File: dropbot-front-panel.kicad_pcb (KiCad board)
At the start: 4 copper layers, 108 x 68.8 mm, 22 parts, among them P1 SFM-105-02-L-D-A, P10 CONN_01X02, P13 CONN_01X01, P14 CONN_01X01, P15 CONN_01X01, P2 SFM-125-02-L-D-A, P3 TFM-125-02-L-DH, P4 SFM-125-02-L-D-A, P5 TFM-125-02-L-DH, P6 SFM-125-02-L-D-A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

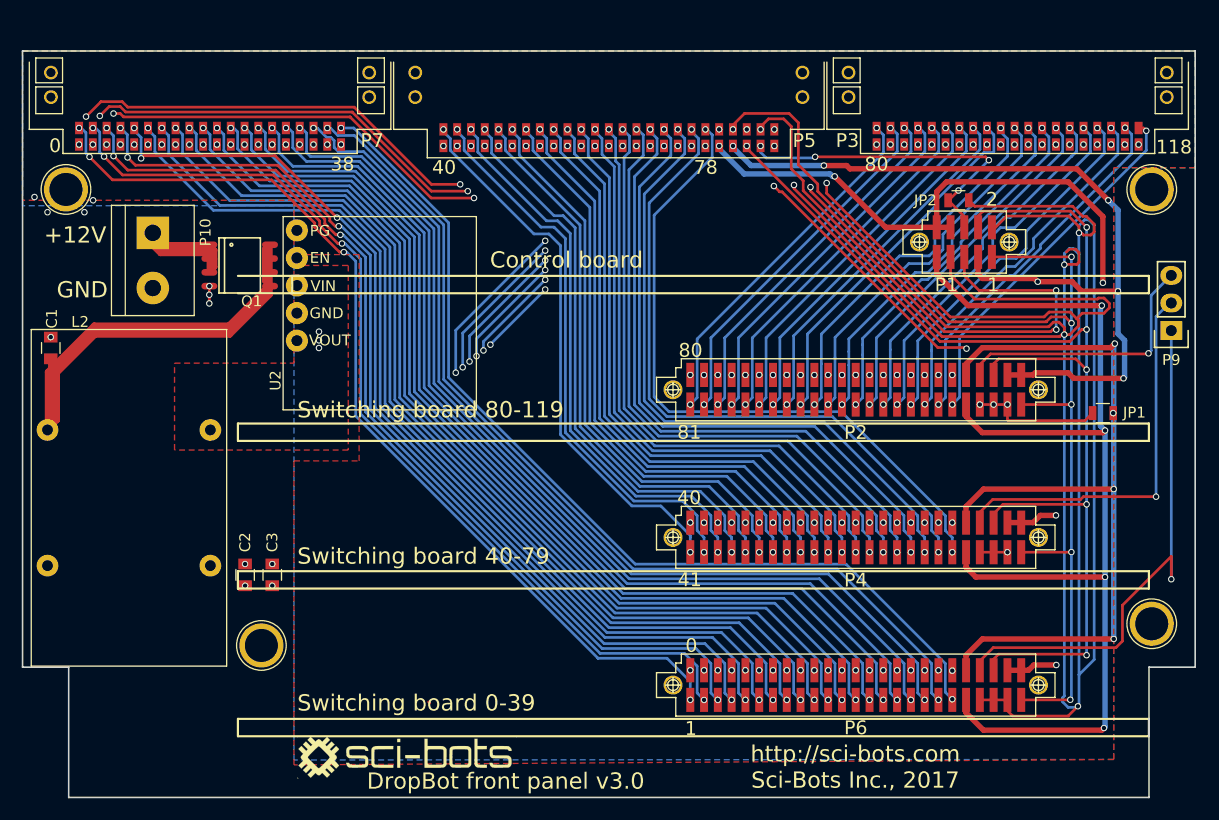
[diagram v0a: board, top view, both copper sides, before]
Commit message: Fix #1, #2 and #3
1. Add i2c EEPROM chip to store serial number, hardware version, etc.
2. Move C2 and C3 (they currently collide with the 2nd switching board)
3. Fix reverse polarity protection
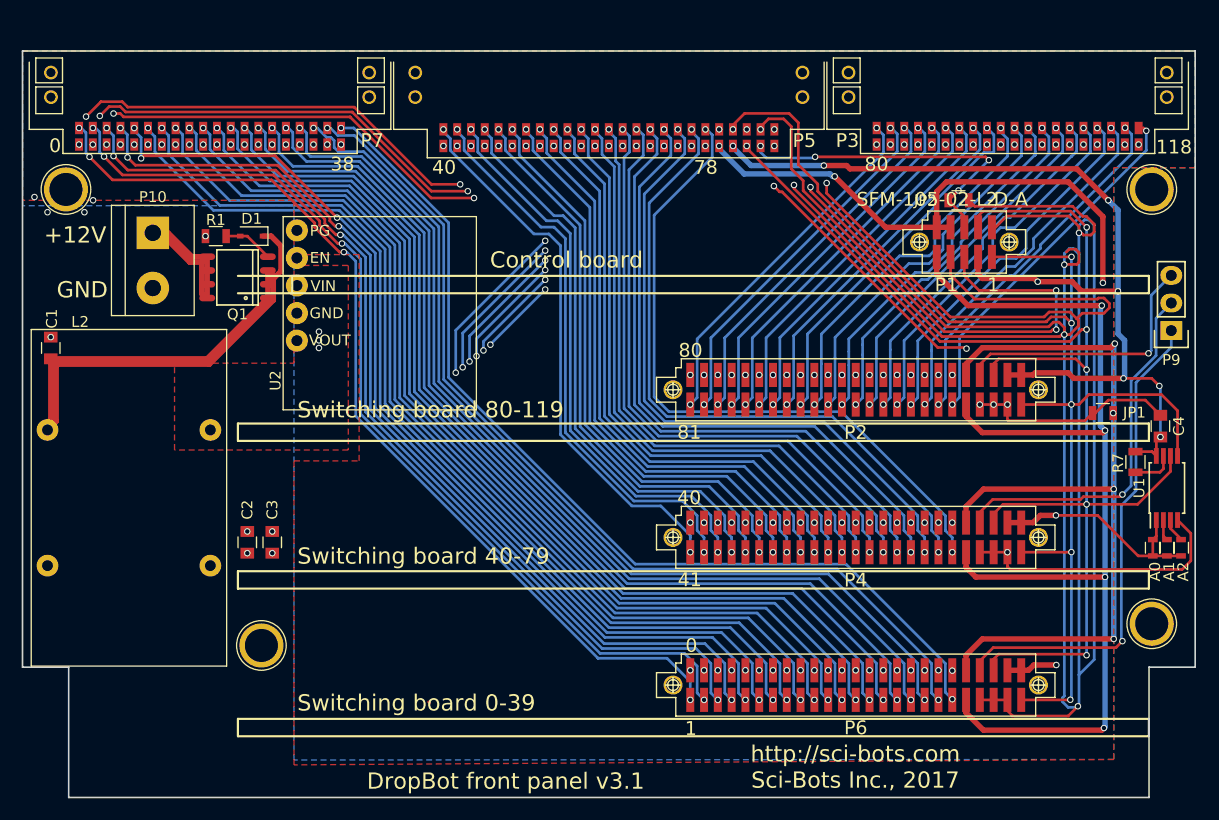
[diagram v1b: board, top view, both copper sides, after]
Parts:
- removed G***: LOGO, WheelerLab:SCI-BOTS-LOGO
- added C4: 0.1uF, Capacitors_SMD:C_0805, F.Cu at (150.8, 65.8)
- added D1: 10V, Diodes_SMD:D_SOD-323, F.Cu at (67.1, 48.3)
- added JP3: A0, Resistors_SMD:R_0603, F.Cu at (150.1, 77.0)
- added JP4: A1, Resistors_SMD:R_0603, F.Cu at (151.4, 77.0)
- added JP5: A2, Resistors_SMD:R_0603, F.Cu at (152.7, 77.0)
- added R1: 10k, Resistors_SMD:R_0805, F.Cu at (63.8, 48.3)
- added R7: 10k, Resistors_SMD:R_0805, F.Cu at (148.5, 69.1)
- added U1: CAT24C__, Housings_SSOP:TSSOP-8_4.4x3mm_Pitch0.65mm, F.Cu at (151.4, 71.5)
- P1: footprint SFM-105-02-XXX-D-A -> WheelerLab:SFM-105-02-XXX-D-A
- P3, P7: value TFM-125-02-L-DH -> TFM-120-02-L-DH
- moved C2 3.01 mm to (66.7, 76.5)
- moved C3 3.00 mm to (69.0, 76.5)
- moved Q1 1.12 mm to (65.8, 52.1), turned to 90 degrees
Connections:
- Q1 pad 1: +12V_SUPPLY -> Net-(C1-Pad1)
- Q1 pad 2: +12V_SUPPLY -> Net-(C1-Pad1)
- Q1 pad 3: +12V_SUPPLY -> Net-(C1-Pad1)
- Q1 pad 4: CHASIS_GND -> Net-(D1-Pad2)
- Q1 pad 5: Net-(C1-Pad1) -> +12V_SUPPLY
- Q1 pad 6: Net-(C1-Pad1) -> +12V_SUPPLY
- Q1 pad 7: Net-(C1-Pad1) -> +12V_SUPPLY
- Q1 pad 8: Net-(C1-Pad1) -> +12V_SUPPLY
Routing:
- net GND: track 300.1 -> 330.3 mm
- net +3.3V: track 94.6 -> 123.4 mm, vias 11 -> 13
- net Net-(C1-Pad1): track 96.7 -> 71.8 mm
- net SDA: track 105.1 -> 120.1 mm
- net SCL: track 123.1 -> 133.5 mm
- net Net-(D1-Pad2): track 0.00 -> 4.63 mm
- net RST1: track 50.4 -> 46.2 mm
- net Net-(R7-Pad2): track 0.00 -> 3.88 mm
- net +12V_SUPPLY: track 24.1 -> 20.3 mm
- net Net-(JP5-Pad2): track 0.00 -> 2.20 mm
- net RST2: track 36.3 -> 34.3 mm
- net Net-(JP4-Pad2): track 0.00 -> 1.93 mm
- net CHASIS_GND: track 13.2 -> 11.4 mm, vias 10 -> 8
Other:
- net class Default: clearance 0.2 -> 0.16
- rule trace_clearance: 0.2 -> 0.16
- board text added: "DropBot front panel v3.1"
- board text removed: "DropBot front panel v3.0"

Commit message: Update to use Sci-Bots library
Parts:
- L2: footprint WheelerLab:RN242-X-02-XXX -> Sci-Bots:RN242-X-02-XXX
- P1: footprint WheelerLab:SFM-105-02-XXX-D-A -> Sci-Bots:SFM-105-02-XXX-D-A
- P10: value CONN_01X02 -> Conn_01x02
- P13, P14, P15, P8: value CONN_01X01 -> Conn_01x01
- P2, P4, P6: footprint WheelerLab:SFM-125-02-XXX-D-A -> Sci-Bots:SFM-125-02-XXX-D-A
- P3, P7: footprint WheelerLab:TFM-120-02-X-DH -> Sci-Bots:TFM-120-02-X-DH
- P5: footprint WheelerLab:TFM-125-02-X-DH -> Sci-Bots:TFM-125-02-X-DH
- P9: value CONN_01X03 -> Conn_01x03
- U2: footprint WheelerLab:D24V22F -> Sci-Bots:D24V22F
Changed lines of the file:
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@@
-(kicad_pcb (version 4) (host pcbnew 4.0.6)
+(kicad_pcb (version 4) (host pcbnew 4.0.7)
   (general
     (links 217)
@@
   (layers
     (0 F.Cu signal)
-    (1 PWR power)
-    (2 GND power)
+    (1 PWR power hide)
+    (2 GND power hide)
     (31 B.Cu signal)
     (32 B.Adhes user)
@@
     (add_net "Net-(C1-Pad1)")
   )
-  (module WheelerLab:RN242-X-02-XXX (layer F.Cu)
+  (module Sci-Bots:RN242-X-02-XXX (layer F.Cu)
     (at 55.8 72.4)
     (fp_text reference L2 (at -4.5 -16.2) (layer F.SilkS)
@@
       (effects (font (size 1 1) (thickness 0.15)))
     )
-    (fp_text value CONN_01X03 (at 2.2 2.7 270) (layer F.Fab) hide
+    (fp_text value Conn_01x03 (at 2.2 2.7 270) (layer F.Fab) hide
       (effects (font (size 1 1) (thickness 0.15)))
     )
@@
     )
   )
-  (module WheelerLab:TFM-120-02-X-DH (layer F.Cu)
+  (module Sci-Bots:TFM-120-02-X-DH (layer F.Cu)
     (at 63.2716 31.7638)
     (descr "0.050\" DOUBLE HORIZONTAL TERMINAL STRIP.")
@@
       (net 2 GND))
   )
-  (module WheelerLab:TFM-120-02-X-DH (layer F.Cu)
+  (module Sci-Bots:TFM-120-02-X-DH (layer F.Cu)
     (at 136.7284 31.7638)
     (descr "0.050\" DOUBLE HORIZONTAL TERMINAL STRIP.")
@@
       (effects (font (size 1 1) (thickness 0.15)))
     )
-    (fp_text value CONN_01X02 (at 2.2 6.4 270) (layer F.Fab) hide
+    (fp_text value Conn_01x02 (at 2.2 6.4 270) (layer F.Fab) hide
       (effects (font (size 1 1) (thickness 0.15)))
     )
@@
     )
   )
-  (module WheelerLab:TFM-125-02-X-DH (layer F.Cu)
+  (module Sci-Bots:TFM-125-02-X-DH (layer F.Cu)
     (at 100 31.7638)
     (descr "0.050\" DOUBLE HORIZONTAL TERMINAL STRIP.")
@@
     )
   )
-  (module WheelerLab:D24V22F (layer F.Cu)
+  (module Sci-Bots:D24V22F (layer F.Cu)
     (at 70 46.5 270)
     (fp_text reference U2 (at 15.1 0.7 450) (layer F.SilkS)
@@
       (effects (font (size 1 1) (thickness 0.15)))
     )
-    (fp_text value CONN_01X01 (at 1.1 3.3) (layer F.Fab) hide
+    (fp_text value Conn_01x01 (at 1.1 3.3) (layer F.Fab) hide
       (effects (font (size 1 1) (thickness 0.15)))
     )
@@
       (effects (font (size 1 1) (thickness 0.15)))
     )
-    (fp_text value CONN_01X01 (at -0.7 3) (layer F.Fab) hide
+    (fp_text value Conn_01x01 (at -0.7 3) (layer F.Fab) hide
       (effects (font (size 1 1) (thickness 0.15)))
     )
@@
       (effects (font (size 1 1) (thickness 0.15)))
     )
-    (fp_text value CONN_01X01 (at -0.6 3.1) (layer F.Fab) hide
+    (fp_text value Conn_01x01 (at -0.6 3.1) (layer F.Fab) hide
       (effects (font (size 1 1) (thickness 0.15)))
     )
@@
       (effects (font (size 1 1) (thickness 0.15)))
     )
-    (fp_text value CONN_01X01 (at 0 3) (layer F.Fab) hide
+    (fp_text value Conn_01x01 (at 0 3) (layer F.Fab) hide
       (effects (font (size 1 1) (thickness 0.15)))
     )
@@
       (net 133 CHASIS_GND))
   )
-  (module WheelerLab:SFM-125-02-XXX-D-A (layer F.Cu)
+  (module Sci-Bots:SFM-125-02-XXX-D-A (layer F.Cu)
     (at 122.7384 62.449)
     (descr "0.05\"X0.05\" SOCKET STRIP DOUBLE ROW ASSEMBLY.")
@@
     (pad "" thru_hole circle (at 16.8275 0) (size 1.75 1.75) (drill 1.27) (layers *.Cu *.Mask F.SilkS))
   )
-  (module WheelerLab:SFM-125-02-XXX-D-A (layer F.Cu)
+  (module Sci-Bots:SFM-125-02-XXX-D-A (layer F.Cu)
     (at 122.7384 76.049)
     (descr "0.05\"X0.05\" SOCKET STRIP DOUBLE ROW ASSEMBLY.")
@@
     (pad "" thru_hole circle (at 16.8275 0) (size 1.75 1.75) (drill 1.27) (layers *.Cu *.Mask F.SilkS))
   )
-  (module WheelerLab:SFM-125-02-XXX-D-A (layer F.Cu)
+  (module Sci-Bots:SFM-125-02-XXX-D-A (layer F.Cu)
     (at 122.7384 89.649)
     (descr "0.05\"X0.05\" SOCKET STRIP DOUBLE ROW ASSEMBLY.")
@@
     )
   )
-  (module WheelerLab:SFM-105-02-XXX-D-A (layer F.Cu)
+  (module Sci-Bots:SFM-105-02-XXX-D-A (layer F.Cu)
     (at 132.7384 48.8495)
     (descr "0.05\"X0.05\" SOCKET STRIP DOUBLE ROW ASSEMBLY.")

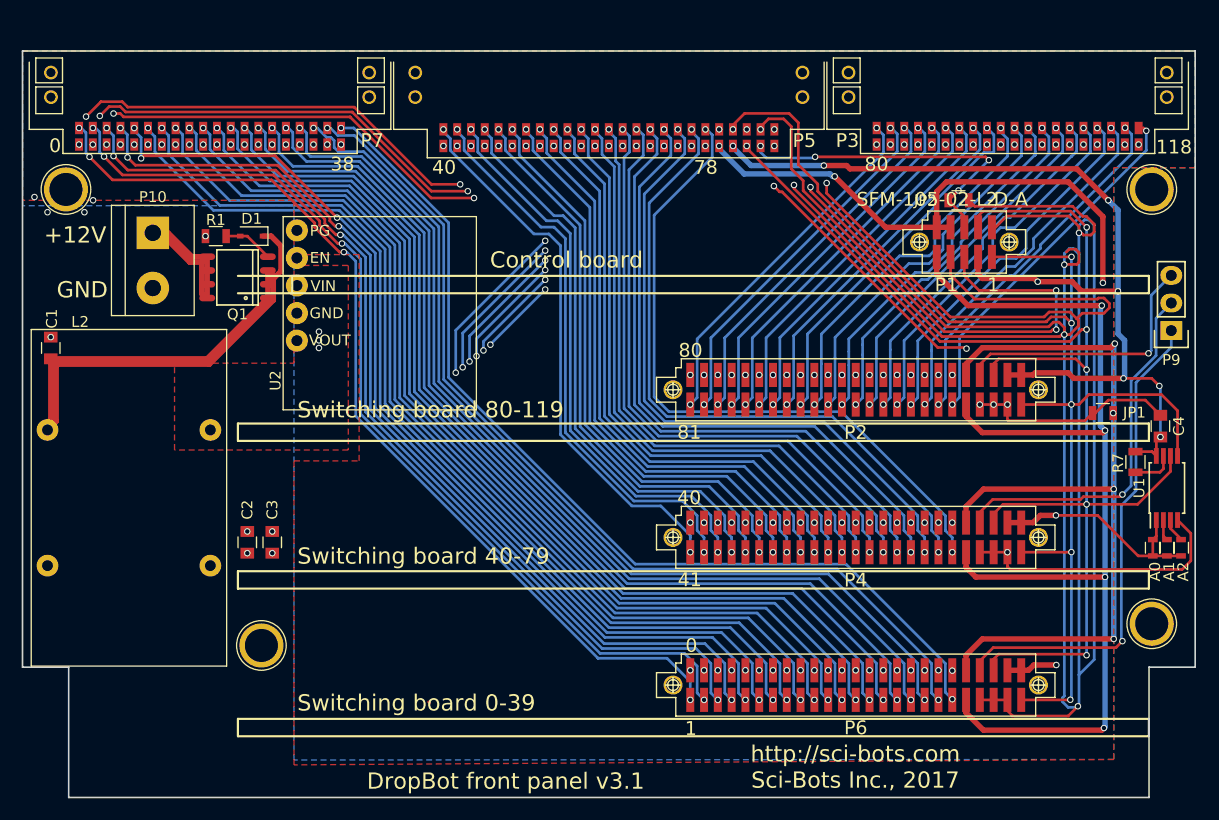
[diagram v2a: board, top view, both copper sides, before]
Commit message: Use through-hole connectors to pogo-pin board
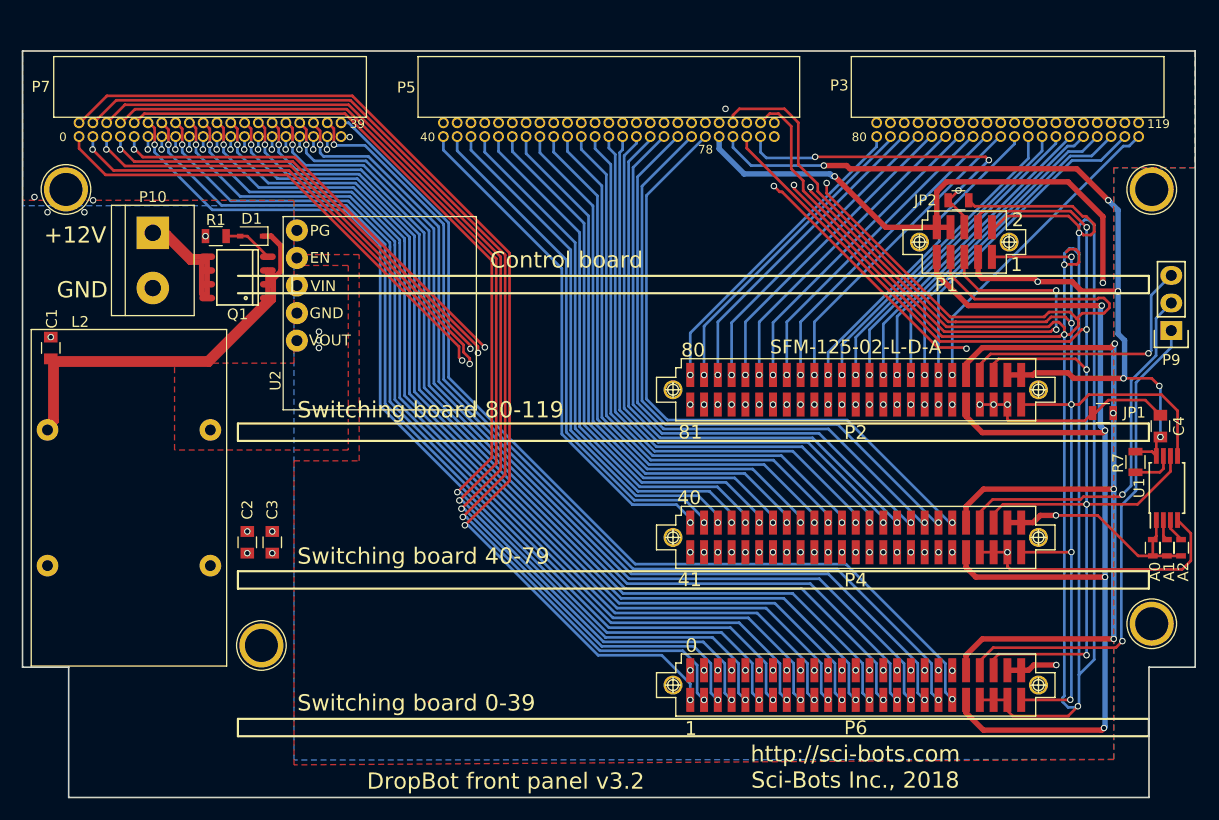
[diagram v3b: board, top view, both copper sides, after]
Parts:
- P3, P7: value TFM-120-02-L-DH -> TFM-120-01-L-D-RA; footprint Sci-Bots:TFM-120-02-X-DH -> Sci-Bots:TFM-120-01-XXX-D-RA
- P5: value TFM-125-02-L-DH -> TFM-125-01-L-D-RA; footprint Sci-Bots:TFM-125-02-X-DH -> Sci-Bots:TFM-125-01-XXX-D-RA
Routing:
- net HVOUT0: track 106.0 -> 85.2 mm, vias 6 -> 2
- net HVOUT2: track 104.2 -> 85.3 mm, vias 6 -> 3
- net HVOUT4: track 102.3 -> 85.3 mm, vias 6 -> 3
- net HVOUT6: track 100.9 -> 85.3 mm, vias 4 -> 3
- net HVOUT8: track 98.8 -> 85.5 mm, vias 4 -> 3
- net HVOUT1: track 88.8 -> 101.8 mm, vias 4 -> 2
- net HVOUT3: track 89.2 -> 101.2 mm, vias 4 -> 2
- net HVOUT10: track 97.0 -> 85.4 mm, vias 4 -> 2
- net HVOUT5: track 89.4 -> 100.0 mm, vias 4 -> 2
- net HVOUT7: track 89.5 -> 98.8 mm, vias 4 -> 2
- net HVOUT9: track 89.7 -> 97.6 mm, vias 4 -> 2
- net GND: track 330.3 -> 334.8 mm, vias 14 -> 13
- net HVOUT78: track 56.6 -> 59.3 mm, vias 2 -> 1
- net HVOUT68: track 51.4 -> 54.0 mm, vias 2 -> 1
- net HVOUT74: track 54.5 -> 57.1 mm, vias 2 -> 1
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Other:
- board text added: "0"
- board text added: "119"
- board text added: "39"
- board text added: "40"
- board text added: "78"
- board text added: "80"
- board text added: "DropBot front panel v3.2"
- board text added: "http://sci-bots.com Sci-Bots Inc., 2018"
- board text removed: "DropBot front panel v3.1"
- board text removed: "http://sci-bots.com Sci-Bots Inc., 2017"

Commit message: Update routing of TFM connectors, replace eeprom part
Fixes #4
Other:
- net class Default: clearance 0.16 -> 0.15; trace_width 0.25 -> 0.15
- net class PWR: clearance 0.2 -> 0.15
- rule trace_clearance: 0.16 -> 0.15
- rule trace_min: 0.2 -> 0.15
- board text added: "DropBot front panel v3.3"
- board text removed: "DropBot front panel v3.2"
